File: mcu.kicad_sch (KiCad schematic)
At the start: 108 parts, among them Q1 IRL6283M, Q10 IRL6283M, Q11 IRL6283M, Q12 IRL6283M, Q13 IRL6283M, Q6 IRL6283M, Q7 IRL6283M, Q8 IRL6283M, Q9 IRL6283M, U9 NUCLEOH723ZG

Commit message: Finished up schematic? - Added missing PSU lines
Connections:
- net NRST: no longer names the net of U9.CN8_5 (NRST_CN8)
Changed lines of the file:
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@@
 	(wire
 		(pts
-			(xy 49.53 133.35) (xy 72.39 133.35)
+			(xy 231.14 146.05) (xy 242.57 146.05)
 		)
 		(stroke
@@
 	(wire
 		(pts
-			(xy 231.14 146.05) (xy 242.57 146.05)
+			(xy 91.44 316.23) (xy 93.98 316.23)
 		)
 		(stroke
@@
 		)
 	)
-	(wire
-		(pts
-			(xy 91.44 316.23) (xy 93.98 316.23)
-		)
-		(stroke
-			(width 0)
-			(type default)
-		)
-	)
 	(global_label "GPIO_PD4"
 		(shape input)
@@
 				(hide yes)
 			)
-		)
-	)
-	(global_label "NRST"
-		(shape input)
-		(at 49.53 133.35 180)
-		(fields_autoplaced yes)
-		(effects
-			(font
-				(size 1.27 1.27)
-			)
-			(justify right)
-		)
-		(property "Intersheetrefs" "${INTERSHEET_REFS}"
-			(at 41.7672 133.35 0)
-			(effects
-				(font
-					(size 1.27 1.27)
-				)
-				(justify right)
-				(hide yes)
-			)

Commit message: Start working on ERC, properly annotate DNP elements
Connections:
- no-connect marks 2 -> 170

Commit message: Fix ERC
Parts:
- added R47: 0R, symbol Device:R
- added R48: DNP, symbol Device:R
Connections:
- net +5V: now also R47.2; no longer U9.CN8_9 (5V_CN8)
- net at U9.CN8_15 (VIN_CN8): now also R48.1
- new net: R47.1, U9.CN8_9 (5V_CN8)
- new net +8V: R48.2
- no-connect marks 170 -> 169

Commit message: Add all footprints
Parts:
- removed Q1, Q10, Q11, Q12, Q13, Q6, Q7, Q8, Q9: IRL6283M, symbol Transistor_FET:IRL6283M
- added Q1, Q2, Q3, Q4, Q5, Q6, Q7, Q8, Q9: 2N7002, Package_TO_SOT_SMD:SOT-23, symbol Transistor_FET:2N7002
- D3: renamed from D6; footprint Diode_THT:D_DO-41_SOD81_P10.16mm_Horizontal -> LED_SMD:LED_0805_2012Metric
- D4: renamed from D7; footprint Diode_THT:D_DO-41_SOD81_P10.16mm_Horizontal -> LED_SMD:LED_0805_2012Metric
- D5: renamed from D8; footprint Diode_THT:D_DO-41_SOD81_P10.16mm_Horizontal -> LED_SMD:LED_0805_2012Metric
- R75: renamed from R48; footprint (none) -> Resistor_SMD:R_0805_2012Metric
- R76: renamed from R47; footprint (none) -> Resistor_SMD:R_0805_2012Metric
- renumbered D13 to D10, D14 to D11, D9 to D6, D10 to D7, D11 to D8, D12 to D9, R167 to R100, R168 to R101, R169 to R102, R75 to R103, R77 to R104, R78 to R105, R120 to R106, R121 to R107, R79 to R108, R80 to R109, R81 to R110, R122 to R111, R124 to R112, R125 to R113, R126 to R114, R127 to R115, R88 to R116, R89 to R117, R90 to R118, R91 to R119, R74 to R120, R133 to R121, R147 to R122, R134 to R123, R151 to R124, R135 to R125, R153 to R126, R136 to R127, R155 to R128, R154 to R129, R139 to R130, R156 to R131, R172 to R132, R140 to R133, R92 to R134, R157 to R135, R158 to R136, R73 to R137, R148 to R138, R149 to R139, R150 to R140, R152 to R141, R82 to R142, R141 to R143, R142 to R144, R143 to R145, R144 to R146, R145 to R147, R146 to R148, R93 to R149, R95 to R150, R96 to R151, R97 to R152, R98 to R153, R99 to R154, R100 to R155, R166 to R65, R173 to R66, R189 to R67, R190 to R68, R191 to R69, R192 to R70, R174 to R71, R183 to R72, R188 to R73, R64 to R74, R85 to R77, R86 to R78, R87 to R79, R178 to R80, R162 to R81, R179 to R82, R119 to R83, R175 to R84, R123 to R85, R176 to R86, R129 to R87, R177 to R88, R128 to R89, R165 to R90, R130 to R91, R163 to R92, R137 to R93, R131 to R94, R164 to R95, R138 to R96, R132 to R97, R170 to R98, R171 to R99, U9 to U11
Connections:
- net AC_DC_CH1: now also Q8.3 (D)
- net AC_DC_CH2: now also Q9.3 (D)
- net CH1_ATTEN_A: now also Q4.3 (D)
- net CH1_ATTEN_B: now also Q5.3 (D)
- net CH2_ATTEN_A: now also Q6.3 (D)
- net CH2_ATTEN_B: now also Q7.3 (D)
- net GND: now also Q1.2 (S), Q2.2 (S), Q3.2 (S), Q4.2 (S), Q5.2 (S), Q6.2 (S), Q7.2 (S), Q8.2 (S), Q9.2 (S)
- net TRIGGER_AC_DC: now also Q3.3 (D)
- net TRIGG_1: now also Q1.3 (D)
- net TRIGG_2: now also Q2.3 (D)
- net at R152.1, R153.1: now also Q8.1 (G)
- net at R116.1, R117.1: now also Q4.1 (G)
- net at R78.1, R79.1: now also Q3.1 (G)
- net at R74.1, R77.1: now also Q2.1 (G)
- net at R118.1, R119.1: now also Q5.1 (G)
- net at R134.1, R149.1: now also Q6.1 (G)
- net at R72.1, R73.1: now also Q1.1 (G)
- net at R154.1, R155.1: now also Q9.1 (G)
- net at R150.1, R151.1: now also Q7.1 (G)

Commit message: Apply changes after review, left to fix: comparator histeresis, PSU missing lines?
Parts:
- removed D7, D9: 1N4001, Diode_THT:D_DO-41_SOD81_P10.16mm_Horizontal, symbol Diode:1N4001
- removed Q5, Q7: 2N7002, Package_TO_SOT_SMD:SOT-23, symbol Transistor_FET:2N7002
- removed R100, R101, R102, R103, R104, R105, R106, R107, R108, R109, R110, R111, R112, R113, R114, R115, R135, R136, R137, R138, R139, R140, R141, R142, R143, R144, R145, R146, R147, R148, R98, R99: 33R, Resistor_SMD:R_0805_2012Metric, symbol Device:R
- removed R118, R150: 220R, Resistor_SMD:R_0805_2012Metric, symbol Device:R
- removed R119, R151: 10k, Resistor_SMD:R_0805_2012Metric, symbol Device:R
- removed R120, R121, R122, R123, R124, R125, R126, R127, R128, R129, R130, R131, R132, R133, R66, R67, R68, R69, R70, R71, R80, R81, R82, R83, R84, R85, R86, R87, R88, R89, R90, R91, R92, R94, R95, R97: 10kR, Resistor_SMD:R_0805_2012Metric, symbol Device:R
- added R56: 10kR, Resistor_SMD:R_0805_2012Metric, symbol Device:R
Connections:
- net +5V is gone; now on net +5V_EXT: R76.2
- net +3V3: now also R56.2
- net DAC_ALM: now also R56.1
- net DAC_TEMP: now also U11.CN9_1 (A0/ADC12_INP15); no longer U11.CN9_19 (D69/I2C_B_SCL)
- net GPIO_0: now also U11.CN10_8 (D4/IO)
- net GPIO_1: now also U11.CN10_31 (D33/TIMER_D_PWM1)
- net GPIO_2: now also U11.CN10_34 (D35/TIMER_C_PWM3)
- net GPIO_3: now also U11.CN10_32 (D36/TIMER_C_PWM2)
- net GPIO_4: now also U11.CN10_29 (D32/TIMER_C_PWM1)
- net GPIO_PD0: now also U11.CN9_19 (D69/I2C_B_SCL)
- net GPIO_PD1: now also U11.CN9_21 (D68/I2C_B_SDA)
- net GPIO_PD3: now also U11.CN9_10 (D55/USART_B_CTS)
- net GPIO_PD4: now also U11.CN9_8 (D54/USART_B_RTS)
- net GPIO_PD5: now also U11.CN9_6 (D53/USART_B_TX)
- net GPIO_PD6: now also U11.CN9_4 (D52/USART_B_RX)
- net GPIO_PD7: now also U11.CN9_2 (D51/USART_B_SCLK)
- net GPIO_PE0: now also U11.CN10_33 (D34/TIMER_B_ETR)
- net GPIO_PE10: now also U11.CN10_24 (D40/TIMER_A_PWM2N)
- net GPIO_PE11: now also U11.CN10_6 (D5/TIMER_A_PWM2)
- net GPIO_PE12: now also U11.CN10_26 (D39/TIMER_A_PWM3N)
- net GPIO_PE13: now also U11.CN10_10 (D3/TIMER_A_PWM3)
- net GPIO_PE15: now also U11.CN10_30 (D37/TIMER_A_BKIN1)
- net GPIO_PE4: now also U11.CN9_16 (D57/SAI_A_FS)
- net GPIO_PE5: now also U11.CN9_18 (D58/SAI_A_SCK)
- net GPIO_PE6: now also U11.CN9_20 (D59/SAI_A_SD)
- net GPIO_PE7: now also U11.CN10_20 (D41/TIMER_A_ETR)
- net GPIO_PE8: now also U11.CN10_18 (D42/TIMER_A_PWM1N)
- net GPIO_PE9: now also U11.CN10_4 (D6/TIMER_A_PWM1)
- net QSPI_CLK: now also U11.CN10_15 (D27/QSPI_CLK)
- net QSPI_CS: now also U11.CN10_13 (D26/QSPI_CS)
- net QSPI_IO0/GPIO_PD11: now also U11.CN10_23 (D30/QSPI_BK1_IO0)
- net QSPI_IO1/GPIO_PD12: now also U11.CN10_21 (D29/QSPI_BK1_IO1)
- net QSPI_IO2/GPIO_PE2: now also U11.CN10_25 (D31/QSPI_BK1_IO2)
- net QSPI_IO3/GPIO_PD13: now also U11.CN10_19 (D28/QSPI_BK1_IO3)
- net USART_1_RX: now also U11.CN10_16 (D0/USART_A_RX)
- net USART_1_TX: now also U11.CN10_14 (D1/USART_A_TX)
- net CH1_ATTEN_A renamed CH1_ATTEN
- net CH1_ATTEN_A_MCU renamed CH1_ATTEN_MCU
- net CH1_ATTEN_B_MCU: no longer names the net of U11.CN7_13 (D22/I2S_B_SD/SPI_B_MOSI)
- net CH2_ATTEN_A renamed CH2_ATTEN
- net CH2_ATTEN_A_MCU renamed CH2_ATTEN_MCU
- net CH2_ATTEN_B_MCU: no longer names the net of U11.CN7_17 (D24/SPI_B_NSS)
- no-connect marks 169 -> 171
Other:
- moved on the sheet: D10, D11, D3, D4, D5, D6, D8, Q1, Q2, Q3, Q4, Q6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

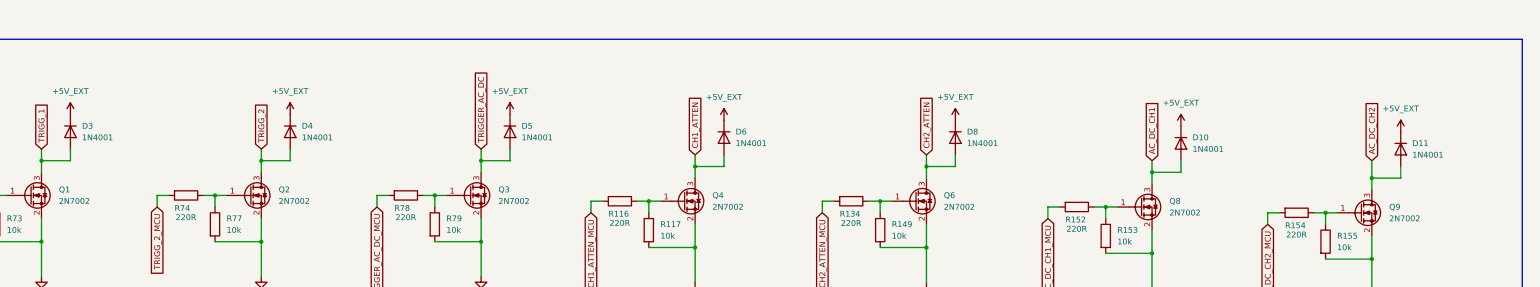
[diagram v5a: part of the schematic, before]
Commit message: Fix footprints and allign components placements
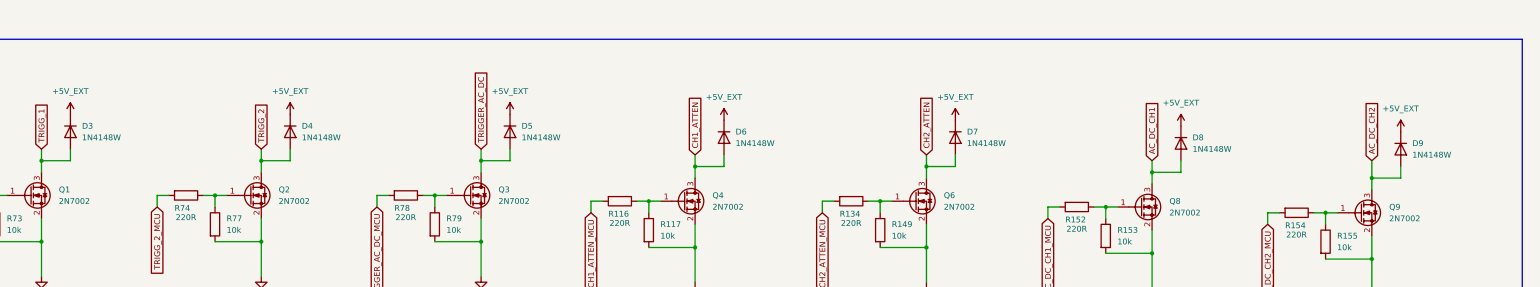
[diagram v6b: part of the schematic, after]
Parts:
- removed D10, D11, D6, D8: 1N4001, Diode_THT:D_DO-41_SOD81_P10.16mm_Horizontal, symbol Diode:1N4001
- removed D3, D4, D5: 1N4001, LED_SMD:LED_0805_2012Metric, symbol Diode:1N4001
- added D3, D4, D5, D6, D7, D8, D9: 1N4148W, Diode_SMD:D_SOD-123, symbol Diode:1N4148W
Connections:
- net +5V_EXT: now also D3.1 (K), D4.1 (K), D5.1 (K), D6.1 (K), D7.1 (K), D8.1 (K), D9.1 (K)
- net AC_DC_CH1: now also D8.2 (A)
- net AC_DC_CH2: now also D9.2 (A)
- net CH1_ATTEN: now also D6.2 (A)
- net CH2_ATTEN: now also D7.2 (A)
- net TRIGGER_AC_DC: now also D5.2 (A)
- net TRIGG_1: now also D3.2 (A)
- net TRIGG_2: now also D4.2 (A)

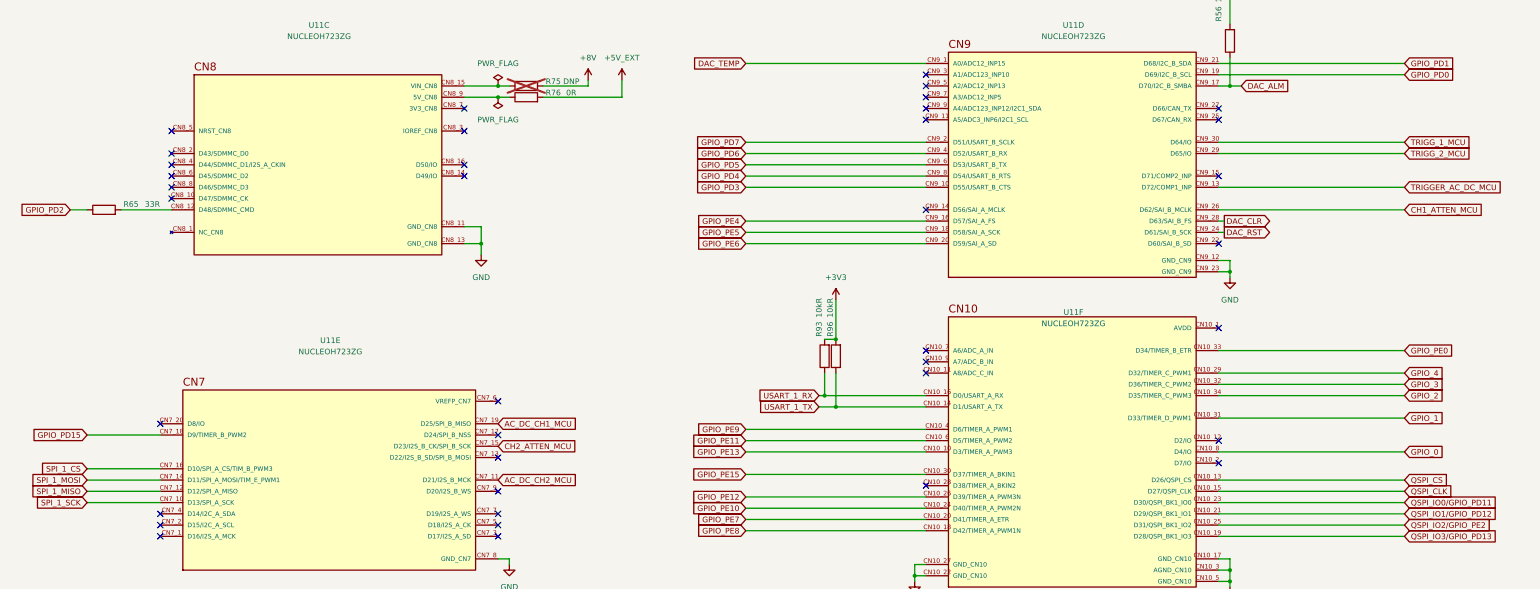
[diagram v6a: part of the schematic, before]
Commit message: Route AFE - attenuators
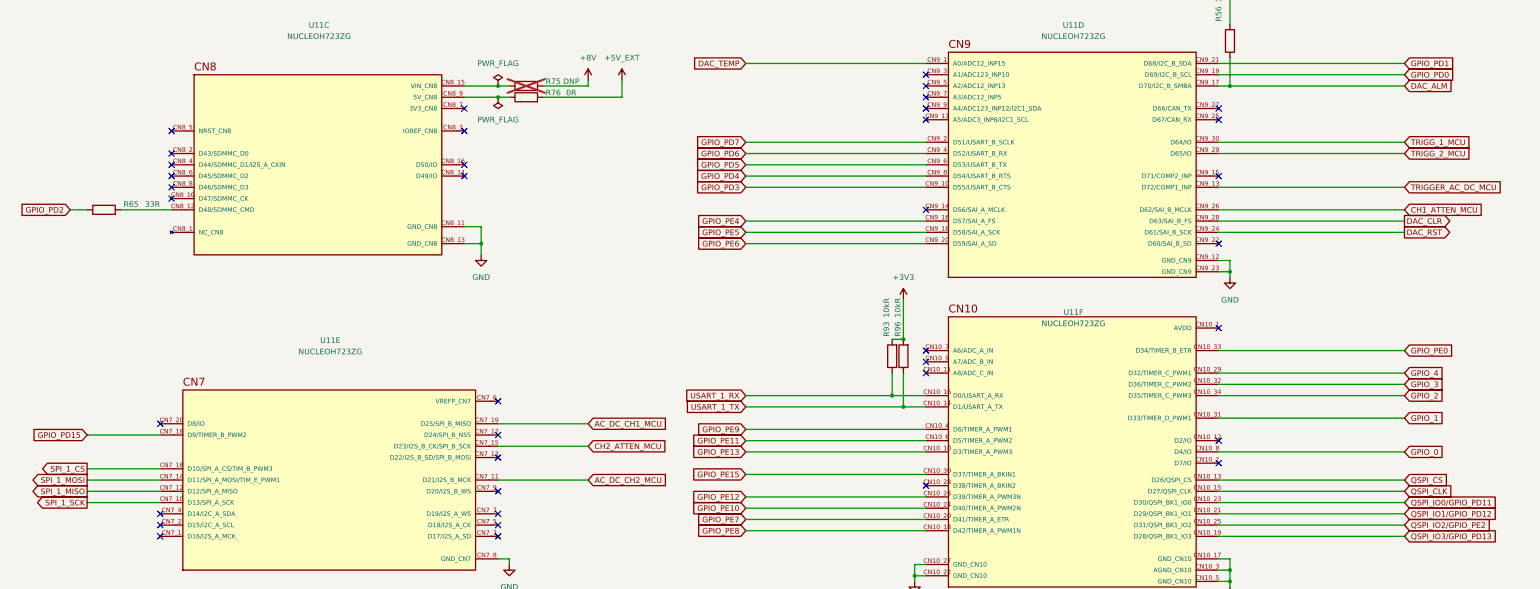
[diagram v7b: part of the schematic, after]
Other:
- moved on the sheet: R93, R96

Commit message: Do most of the PCB
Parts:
- removed unit 10 of U11
- removed unit 1 of U11
- removed unit 2 of U11
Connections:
- net GND: no longer U11.CN10_17 (GND_CN10), U11.CN10_22 (GND_CN10), U11.CN10_27 (GND_CN10), U11.CN10_3 (AGND_CN10), U11.CN10_5 (GND_CN10), U11.CN9_12 (GND_CN9), U11.CN9_23 (GND_CN9)
- net QSPI_CLK: no longer U11.CN10_15 (D27/QSPI_CLK)
- net QSPI_CS: no longer U11.CN10_13 (D26/QSPI_CS)
- net QSPI_IO0/GPIO_PD11: no longer U11.CN10_23 (D30/QSPI_BK1_IO0)
- net QSPI_IO1/GPIO_PD12: no longer U11.CN10_21 (D29/QSPI_BK1_IO1)
- net QSPI_IO2/GPIO_PE2: no longer U11.CN10_25 (D31/QSPI_BK1_IO2)
- net QSPI_IO3/GPIO_PD13: no longer U11.CN10_19 (D28/QSPI_BK1_IO3)
- net at U11.CN3_1 (GND_CN3): no longer U11.CN3_2 (GND_CN3)
- net at U11.CN4_1 (GND_CN4): no longer U11.CN4_2 (GND_CN4)
- new net: U11.CN9_12 (GND_CN9), U11.CN9_23 (GND_CN9)
- new net: U11.CN10_17 (GND_CN10), U11.CN10_22 (GND_CN10), U11.CN10_27 (GND_CN10), U11.CN10_5 (GND_CN10)
- no-connect marks 171 -> 40
